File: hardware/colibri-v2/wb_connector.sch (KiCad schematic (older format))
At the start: 21 parts, among them CN3 AS0B821-S78B-7H, Q13 BSS138PW, U6 M25P32-VME6G

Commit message: Added BMP180_LGA footprint
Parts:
- CN3: footprint (none) -> Sigmadrone:AS0B821-S78B-7H
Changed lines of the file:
@@
 F 0 "CN3" H 6950 10237 60  0000 C CNN
 F 1 "AS0B821-S78B-7H" H 6950 10131 60  0000 C CNN
-F 2 "" H 6950 6000 60  0001 C CNN
+F 2 "Sigmadrone:AS0B821-S78B-7H" H 6950 6000 60  0001 C CNN
 F 3 "" H 6950 6000 60  0000 C CNN
 	1    6950 5750

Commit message: Added and assigned footprints.
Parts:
- CN3: footprint (none) -> Sigmadrone:AS0B821-S78B-7H
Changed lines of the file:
@@
 F 0 "CN3" H 12700 10237 60  0000 C CNN
 F 1 "AS0B821-S78B-7H" H 12700 10131 60  0000 C CNN
-F 2 "" H 12700 6000 60  0001 C CNN
+F 2 "Sigmadrone:AS0B821-S78B-7H" H 12700 6000 60  0001 C CNN
 F 3 "" H 12700 6000 60  0000 C CNN
 	2    12700 5750

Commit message: Adding and assigning footprints
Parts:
- Q13: footprint (none) -> TO_SOT_Packages_SMD:SOT-323
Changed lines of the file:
@@
 F 0 "Q13" H 9950 13050 50  0000 R CNN
 F 1 "BSS138PW" H 9650 13200 50  0000 R CNN
-F 2 "" H 9850 13100 29  0001 C CNN
+F 2 "TO_SOT_Packages_SMD:SOT-323" H 9850 13100 29  0001 C CNN
 F 3 "" H 9650 13000 60  0000 C CNN
 	1    9650 13000

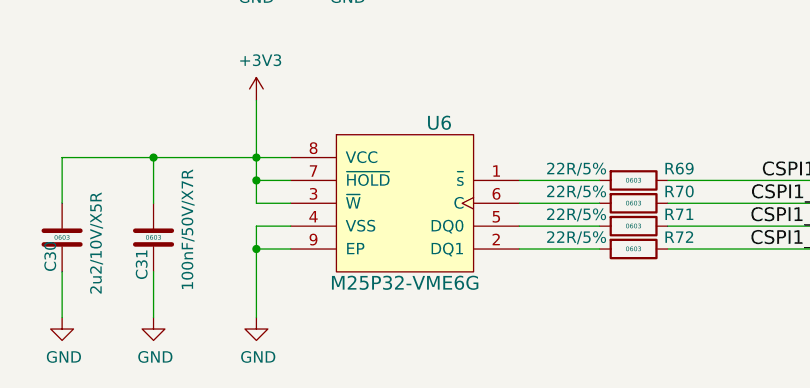
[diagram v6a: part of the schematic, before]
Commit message: Added footprints
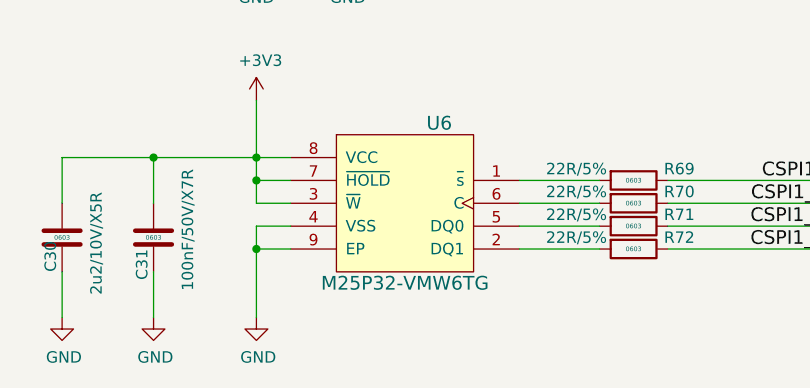
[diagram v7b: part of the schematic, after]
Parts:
- U6: value M25P32-VME6G -> M25P32-VMW6TG; Part (none) -> 557-1635-1-ND; Provider (none) -> Digikey
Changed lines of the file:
@@
 P 10000 14550
 F 0 "U6" H 10150 14900 60  0000 C CNN
-F 1 "M25P32-VME6G" H 10000 14200 60  0000 C CNN
+F 1 "M25P32-VMW6TG" H 10000 14200 60  0000 C CNN
 F 2 "" H 10000 14550 60  0001 C CNN
 F 3 "" H 10000 14550 60  0000 C CNN
+F 4 "557-1635-1-ND" H 10000 14550 60  0001 C CNN "Part"
+F 5 "Digikey" H 10000 14550 60  0001 C CNN "Provider"
 	1    10000 14550
 	1    0    0    -1

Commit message: Assigned footprints
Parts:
- U6: footprint (none) -> Housings_SOIC:SOIJ-8_5.3x5.3mm_Pitch1.27mm
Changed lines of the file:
@@
 F 0 "U6" H 10150 14900 60  0000 C CNN
 F 1 "M25P32-VMW6TG" H 10000 14200 60  0000 C CNN
-F 2 "" H 10000 14550 60  0001 C CNN
+F 2 "Housings_SOIC:SOIJ-8_5.3x5.3mm_Pitch1.27mm" H 10000 14550 60  0001 C CNN
 F 3 "" H 10000 14550 60  0000 C CNN
 F 4 "557-1635-1-ND" H 10000 14550 60  0001 C CNN "Part"
